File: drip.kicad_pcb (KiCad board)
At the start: 2 copper layers, 24 parts, among them Q1 2n2222, Q2 2n2222, Q3 2n2222, Q4 2n2222, Q5 2n2222, Q6 2n2222, Q7 2n2222, Q8 2n2222, U1 SA39-12YWA, U2 SA39-12YWA, U3 SA39-12YWA, U4 SA39-12YWA, U5 SA39-12YWA, U6 SA39-12YWA, U7 SA39-12YWA, U8 SA39-12YWA

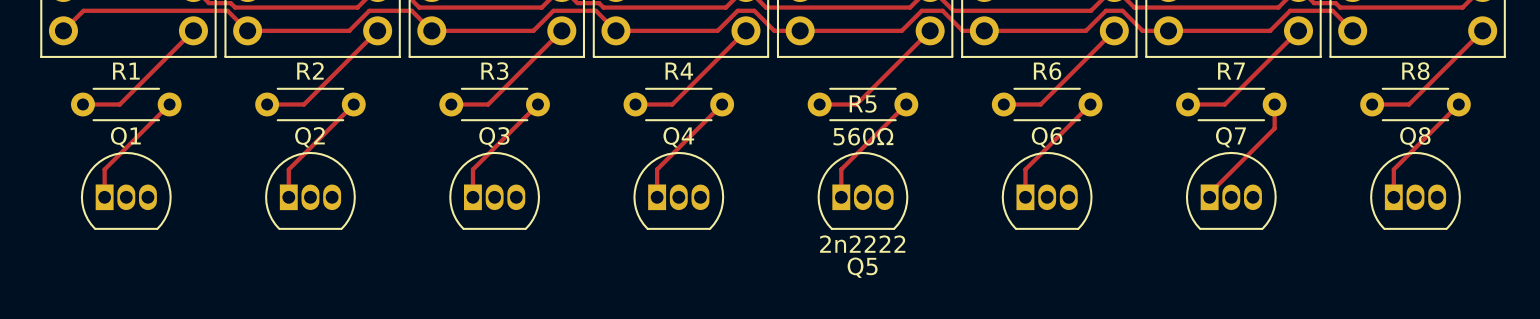
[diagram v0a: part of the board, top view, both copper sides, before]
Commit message: PNP transistors to prepare for '138 based
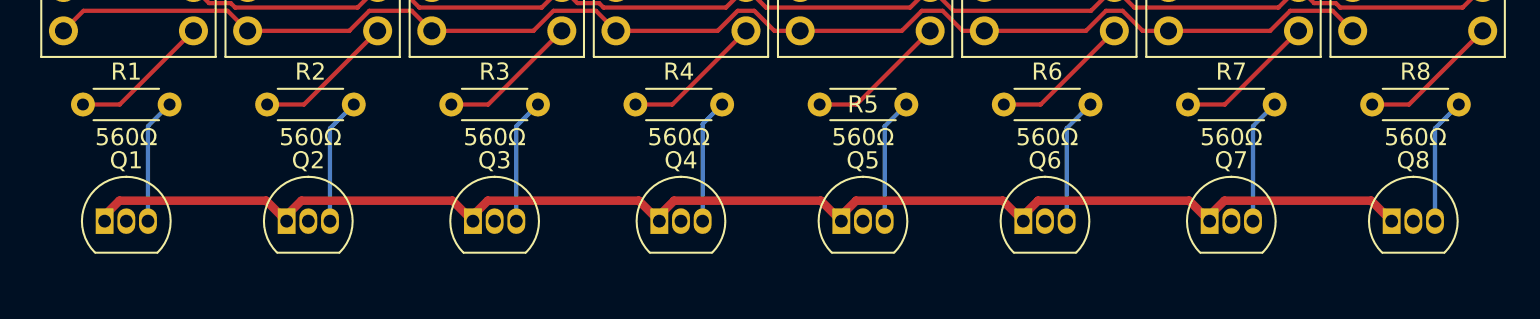
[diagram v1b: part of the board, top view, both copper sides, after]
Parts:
- Q1, Q2, Q3, Q4, Q5, Q6, Q7, Q8: value 2n2222 -> 2n2907
- moved Q2 1.40 mm to (86.9, 53.2)
- moved Q4 1.40 mm to (108.7, 53.2)
- moved Q6 1.40 mm to (130.0, 53.2)
- moved Q8 1.40 mm to (151.6, 53.2)
- moved Q1 1.40 mm to (76.2, 53.2)
- moved Q3 1.40 mm to (97.8, 53.2)
- moved Q5 1.40 mm to (119.4, 53.2)
- moved Q7 1.40 mm to (141.0, 53.2)
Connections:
- net /7SEG_A renamed Net-(R9-Pad2)
- net /7SEG_B renamed Net-(R10-Pad2)
- net /7SEG_C renamed Net-(R11-Pad2)
- net /7SEG_D renamed Net-(R12-Pad2)
- net /7SEG_E renamed Net-(R13-Pad2)
- net /7SEG_F renamed Net-(R14-Pad2)
- net /7SEG_G renamed Net-(R15-Pad2)
- Q1 pad 1: Net-(Q1-Pad1) -> +3V3
- Q1 pad 3: +3V3 -> Net-(Q1-Pad3)
- Q2 pad 1: Net-(Q2-Pad1) -> +3V3
- Q2 pad 3: +3V3 -> Net-(R2-Pad2)
- Q3 pad 1: Net-(Q3-Pad1) -> +3V3
- Q3 pad 3: +3V3 -> Net-(R3-Pad2)
- Q4 pad 1: Net-(Q4-Pad1) -> +3V3
- Q4 pad 3: +3V3 -> Net-(R4-Pad2)
- Q5 pad 1: Net-(Q5-Pad1) -> +3V3
- Q5 pad 3: +3V3 -> Net-(R5-Pad2)
- Q6 pad 1: Net-(Q6-Pad1) -> +3V3
- Q6 pad 3: +3V3 -> Net-(R6-Pad2)
- Q7 pad 1: Net-(Q7-Pad1) -> +3V3
- Q7 pad 3: +3V3 -> Net-(R7-Pad2)
- Q8 pad 1: Net-(Q8-Pad1) -> +3V3
- Q8 pad 3: +3V3 -> Net-(R8-Pad2)
- R1 pad 2: Net-(Q1-Pad1) -> Net-(Q1-Pad3)
- R2 pad 2: Net-(Q2-Pad1) -> Net-(R2-Pad2)
- R3 pad 2: Net-(Q3-Pad1) -> Net-(R3-Pad2)
- R4 pad 2: Net-(Q4-Pad1) -> Net-(R4-Pad2)
- R5 pad 2: Net-(Q5-Pad1) -> Net-(R5-Pad2)
- R6 pad 2: Net-(Q6-Pad1) -> Net-(R6-Pad2)
- R7 pad 2: Net-(Q7-Pad1) -> Net-(R7-Pad2)
- R8 pad 2: Net-(Q8-Pad1) -> Net-(R8-Pad2)
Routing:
- net +3V3: track 0.00 -> 83.8 mm
- net Net-(R6-Pad2): track 0.00 -> 7.42 mm
- net Net-(R2-Pad2): track 0.00 -> 7.42 mm
- net Net-(R8-Pad2): track 0.00 -> 7.42 mm
- net Net-(R7-Pad2): track 0.00 -> 7.36 mm
- net Net-(Q1-Pad3): track 0.00 -> 7.36 mm
- net Net-(R5-Pad2): track 0.00 -> 7.36 mm
- net Net-(R3-Pad2): track 0.00 -> 7.36 mm
- net Net-(R4-Pad2): track 0.00 -> 7.31 mm
- net Net-(Q8-Pad1): track 7.02 -> 0.00 mm
- net Net-(Q7-Pad1): track 7.02 -> 0.00 mm
- net Net-(Q6-Pad1): track 7.02 -> 0.00 mm
- net Net-(Q5-Pad1): track 7.02 -> 0.00 mm
- net Net-(Q4-Pad1): track 7.02 -> 0.00 mm
- net Net-(Q2-Pad1): track 7.02 -> 0.00 mm
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
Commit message: Add a ridiculous logo
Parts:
- added G***: LOGO, Logos:LittleDrip30mm, F.Cu at (78.5, 89.2)
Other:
- board text added: "leadedsolder.com 2023"

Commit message: LED driver done
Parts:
- removed R1, R2, R3, R4, R5, R6, R7, R8: 560Ω, Resistor_THT:R_Axial_DIN0204_L3.6mm_D1.6mm_P5.08mm_Horizontal
- removed U5, U6, U7, U8: SA39-12YWA, Display_7Segment:Sx39-1xxxxx
- added J1: ISP, Connector_PinHeader_2.54mm:PinHeader_1x04_P2.54mm_Vertical, F.Cu at (95.2, 34.9)
- added JP1: Jumper_2_Bridged, Jumper:SolderJumper-2_P1.3mm_Bridged2Bar_RoundedPad1.0x1.5mm, F.Cu at (168.4, 126.5)
- added JP2: Jumper_2_Bridged, Jumper:SolderJumper-2_P1.3mm_Bridged2Bar_RoundedPad1.0x1.5mm, F.Cu at (171.2, 126.5)
- added JP3: Jumper_2_Bridged, Jumper:SolderJumper-2_P1.3mm_Bridged2Bar_RoundedPad1.0x1.5mm, F.Cu at (174.0, 126.5)
- added JP4: Jumper_2_Bridged, Jumper:SolderJumper-2_P1.3mm_Bridged2Bar_RoundedPad1.0x1.5mm, F.Cu at (176.8, 126.5)
- added SW1: 8, Button_Switch_Keyboard:SW_Cherry_MX_1.00u_PCB, F.Cu at (172.1, 43.0)
- added SW10: Divide, Button_Switch_Keyboard:SW_Cherry_MX_1.00u_PCB, F.Cu at (132.4, 56.2)
- added SW11: Divide, Button_Switch_Keyboard:SW_Cherry_MX_1.00u_PCB, F.Cu at (152.6, 63.2)
- added SW12: Divide, Button_Switch_Keyboard:SW_Cherry_MX_1.00u_PCB, F.Cu at (213.2, 56.4)
- added SW2: 5, Button_Switch_Keyboard:SW_Cherry_MX_1.00u_PCB, F.Cu at (183.0, 16.0)
- added SW3: 2, Button_Switch_Keyboard:SW_Cherry_MX_1.00u_PCB, F.Cu at (212.5, 36.2)
- added SW4: Decimal, Button_Switch_Keyboard:SW_Cherry_MX_1.00u_PCB, F.Cu at (223.4, 16.0)
- added SW5: 9, Button_Switch_Keyboard:SW_Cherry_MX_1.00u_PCB, F.Cu at (232.7, 36.2)
- added SW6: 6, Button_Switch_Keyboard:SW_Cherry_MX_1.00u_PCB, F.Cu at (172.8, 63.2)
- added SW7: 3, Button_Switch_Keyboard:SW_Cherry_MX_1.00u_PCB, F.Cu at (193.0, 56.4)
- added SW8: CHS, Button_Switch_Keyboard:SW_Cherry_MX_1.00u_PCB, F.Cu at (192.3, 36.2)
- added SW9: Divide, Button_Switch_Keyboard:SW_Cherry_MX_1.00u_PCB, F.Cu at (203.2, 16.0)
- U1: value SA39-12YWA -> 74LS138; footprint Display_7Segment:Sx39-1xxxxx -> Package_DIP:DIP-16_W7.62mm_Socket_LongPads
- U2, U3: value SA39-12YWA -> 5641AS-4Digit-7Segment; footprint Display_7Segment:Sx39-1xxxxx -> 5641AS:5641AS_THT
- U4: value SA39-12YWA -> MSP430G2553IN20; footprint Display_7Segment:Sx39-1xxxxx -> Package_DIP:DIP-20_W7.62mm
- moved G*** 133.8 mm to (204.9, 133.2)
- moved U1 131.4 mm to (176.8, 113.5), turned to -90 degrees
- moved U3 121.1 mm to (188.6, 109.2)
- moved U4 102.9 mm to (129.5, 132.1), turned to 90 degrees
- moved U2 94.1 mm to (138.1, 109.2)
- moved Q5 88.7 mm to (182.4, 115.6)
- moved Q6 85.1 mm to (188.0, 115.6)
- moved Q1 84.2 mm to (132.7, 115.6)
- moved Q7 81.6 mm to (193.5, 115.6)
- moved Q2 80.8 mm to (138.2, 115.6)
- moved Q8 78.4 mm to (199.1, 115.6)
- moved Q3 77.5 mm to (143.8, 115.6)
- moved Q4 74.4 mm to (149.4, 115.6)
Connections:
- Q1 pad 1: +3V3 -> GND
- Q1 pad 2: unconnected-(Q1-Pad2) -> Net-(Q1-Pad2)
- Q2 pad 1: +3V3 -> GND
- Q2 pad 2: unconnected-(Q2-Pad2) -> Net-(Q2-Pad2)
- Q2 pad 3: Net-(R2-Pad2) -> Net-(Q2-Pad3)
- Q3 pad 1: +3V3 -> GND
- Q3 pad 2: unconnected-(Q3-Pad2) -> Net-(Q3-Pad2)
- Q3 pad 3: Net-(R3-Pad2) -> Net-(Q3-Pad3)
- Q4 pad 1: +3V3 -> GND
- Q4 pad 2: unconnected-(Q4-Pad2) -> Net-(Q4-Pad2)
- Q4 pad 3: Net-(R4-Pad2) -> Net-(Q4-Pad3)
- Q5 pad 1: +3V3 -> GND
- Q5 pad 2: unconnected-(Q5-Pad2) -> Net-(Q5-Pad2)
- Q5 pad 3: Net-(R5-Pad2) -> Net-(Q5-Pad3)
- Q6 pad 1: +3V3 -> GND
- Q6 pad 2: unconnected-(Q6-Pad2) -> Net-(Q6-Pad2)
- Q6 pad 3: Net-(R6-Pad2) -> Net-(Q6-Pad3)
- Q7 pad 1: +3V3 -> GND
- Q7 pad 2: unconnected-(Q7-Pad2) -> Net-(Q7-Pad2)
- Q7 pad 3: Net-(R7-Pad2) -> Net-(Q7-Pad3)
- Q8 pad 1: +3V3 -> GND
- Q8 pad 2: unconnected-(Q8-Pad2) -> Net-(Q8-Pad2)
- Q8 pad 3: Net-(R8-Pad2) -> Net-(Q8-Pad3)
- U1 pad 1: unconnected-(U1-Pad1) -> Net-(JP4-Pad2)
- U1 pad 10: Net-(R9-Pad2) -> Net-(R3-Pad1)
- U1 pad 2: Net-(R14-Pad2) -> Net-(JP3-Pad2)
- U1 pad 3: Net-(R15-Pad2) -> Net-(JP2-Pad2)
- U1 pad 4: Net-(R13-Pad2) -> GND
- U1 pad 5: Net-(R12-Pad2) -> Net-(JP1-Pad2)
- U1 pad 6: Net-(R1-Pad1) -> VCC
- U1 pad 7: GND -> Net-(R1-Pad1)
- U1 pad 8: Net-(R11-Pad2) -> GND
- U1 pad 9: Net-(R10-Pad2) -> Net-(R2-Pad1)
- U2 pad 1: unconnected-(U2-Pad1) -> /d4
- U2 pad 10: Net-(R9-Pad2) -> /d5
- U2 pad 2: Net-(R14-Pad2) -> /d3
- U2 pad 3: Net-(R15-Pad2) -> /d7
- U2 pad 4: Net-(R13-Pad2) -> /d2
- U2 pad 5: Net-(R12-Pad2) -> /d6
- U2 pad 6: Net-(R2-Pad1) -> Net-(Q4-Pad3)
- U2 pad 7: GND -> /d1
- U2 pad 8: Net-(R11-Pad2) -> Net-(Q3-Pad3)
- U2 pad 9: Net-(R10-Pad2) -> Net-(Q2-Pad3)
- U3 pad 1: unconnected-(U3-Pad1) -> /d4
- U3 pad 10: Net-(R9-Pad2) -> /d5
- U3 pad 2: Net-(R14-Pad2) -> /d3
- U3 pad 3: Net-(R15-Pad2) -> /d7
- U3 pad 4: Net-(R13-Pad2) -> /d2
- U3 pad 5: Net-(R12-Pad2) -> /d6
- U3 pad 6: Net-(R3-Pad1) -> Net-(Q8-Pad3)
- U3 pad 7: GND -> /d1
- U3 pad 8: Net-(R11-Pad2) -> Net-(Q7-Pad3)
- U3 pad 9: Net-(R10-Pad2) -> Net-(Q6-Pad3)
- U4 pad 1: unconnected-(U4-Pad1) -> VCC
- U4 pad 10: Net-(R9-Pad2) -> unconnected-(U4-Pad10)
- U4 pad 2: Net-(R14-Pad2) -> /d0
- U4 pad 3: Net-(R15-Pad2) -> /d1
- U4 pad 4: Net-(R13-Pad2) -> /d2
- U4 pad 5: Net-(R12-Pad2) -> /d3
- U4 pad 6: Net-(R4-Pad1) -> /d4
- U4 pad 7: GND -> /d5
- U4 pad 8: Net-(R11-Pad2) -> unconnected-(U4-Pad8)
- U4 pad 9: Net-(R10-Pad2) -> unconnected-(U4-Pad9)
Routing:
- net +3V3: track 83.8 -> 0.00 mm
- net Net-(R10-Pad2): track 82.7 -> 0.00 mm
- net Net-(R15-Pad2): track 82.5 -> 0.00 mm
- net GND: track 82.5 -> 0.00 mm
- net Net-(R9-Pad2): track 82.4 -> 0.00 mm
- net Net-(R12-Pad2): track 82.4 -> 0.00 mm
- net Net-(R13-Pad2): track 82.4 -> 0.00 mm
- net Net-(R11-Pad2): track 82.4 -> 0.00 mm
- net Net-(R14-Pad2): track 82.4 -> 0.00 mm
- net Net-(JP4-Pad2): track 0.00 -> 13.2 mm, vias 0 -> 1
- net Net-(JP3-Pad2): track 0.00 -> 13.1 mm, vias 0 -> 1
- net Net-(JP1-Pad2): track 0.00 -> 13.0 mm, vias 0 -> 1
- net Net-(JP2-Pad2): track 0.00 -> 13.0 mm, vias 0 -> 1
- net Net-(R7-Pad1): track 8.27 -> 0.00 mm
- net Net-(R3-Pad1): track 8.27 -> 0.00 mm
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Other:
- board text added: "5641AS"

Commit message: Button footprint, maybe
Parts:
- added R1: 10kΩ, Resistor_THT:R_Axial_DIN0207_L6.3mm_D2.5mm_P10.16mm_Horizontal, F.Cu at (266.2, 154.0)
- added R10: 10kΩ, Resistor_THT:R_Axial_DIN0207_L6.3mm_D2.5mm_P10.16mm_Horizontal, F.Cu at (292.8, 141.9)
- added R11: 47kΩ, Resistor_THT:R_Axial_DIN0207_L6.3mm_D2.5mm_P10.16mm_Horizontal, F.Cu at (266.2, 145.9)
- added R12: 10kΩ, Resistor_THT:R_Axial_DIN0207_L6.3mm_D2.5mm_P10.16mm_Horizontal, F.Cu at (254.4, 176.1)
- added R13: 10kΩ, Resistor_THT:R_Axial_DIN0207_L6.3mm_D2.5mm_P10.16mm_Horizontal, F.Cu at (266.2, 158.1)
- added R14: 10kΩ, Resistor_THT:R_Axial_DIN0207_L6.3mm_D2.5mm_P10.16mm_Horizontal, F.Cu at (267.8, 150.0)
- added R15: 10kΩ, Resistor_THT:R_Axial_DIN0207_L6.3mm_D2.5mm_P10.16mm_Horizontal, F.Cu at (267.8, 162.1)
- added R16: 10kΩ, Resistor_THT:R_Axial_DIN0207_L6.3mm_D2.5mm_P10.16mm_Horizontal, F.Cu at (254.4, 163.9)
- added R17: 10kΩ, Resistor_THT:R_Axial_DIN0207_L6.3mm_D2.5mm_P10.16mm_Horizontal, F.Cu at (279.5, 141.9)
- added R18: 10kΩ, Resistor_THT:R_Axial_DIN0207_L6.3mm_D2.5mm_P10.16mm_Horizontal, F.Cu at (281.1, 150.0)
- added R19: 10kΩ, Resistor_THT:R_Axial_DIN0207_L6.3mm_D2.5mm_P10.16mm_Horizontal, F.Cu at (254.4, 168.0)
- added R2: 10kΩ, Resistor_THT:R_Axial_DIN0207_L6.3mm_D2.5mm_P10.16mm_Horizontal, F.Cu at (254.4, 180.1)
- added R3: 10kΩ, Resistor_THT:R_Axial_DIN0207_L6.3mm_D2.5mm_P10.16mm_Horizontal, F.Cu at (292.8, 145.9)
- added R4: 10kΩ, Resistor_THT:R_Axial_DIN0207_L6.3mm_D2.5mm_P10.16mm_Horizontal, F.Cu at (254.4, 172.0)
- added R5: 10kΩ, Resistor_THT:R_Axial_DIN0207_L6.3mm_D2.5mm_P10.16mm_Horizontal, F.Cu at (266.2, 141.9)
- added R6: 10kΩ, Resistor_THT:R_Axial_DIN0207_L6.3mm_D2.5mm_P10.16mm_Horizontal, F.Cu at (279.5, 145.9)
- added R7: 10kΩ, Resistor_THT:R_Axial_DIN0207_L6.3mm_D2.5mm_P10.16mm_Horizontal, F.Cu at (279.5, 154.0)
- added R8: 10kΩ, Resistor_THT:R_Axial_DIN0207_L6.3mm_D2.5mm_P10.16mm_Horizontal, F.Cu at (267.8, 170.2)
- added R9: 1kΩ, Resistor_THT:R_Axial_DIN0207_L6.3mm_D2.5mm_P10.16mm_Horizontal, F.Cu at (267.8, 166.2)
- added SW13: 7, DripButtons:8mm_G77_Push, F.Cu at (267.4, 183.4)
- added SW14: 4, DripButtons:8mm_G77_Push, F.Cu at (322.8, 168.8)
- added SW15: 1, DripButtons:8mm_G77_Push, F.Cu at (280.7, 167.2)
- added SW16: 0, DripButtons:8mm_G77_Push, F.Cu at (254.1, 184.3)
- added SW17: Hex, DripButtons:8mm_G77_Push, F.Cu at (337.4, 142.0)
- added SW18: E, DripButtons:8mm_G77_Push, F.Cu at (275.2, 193.9)
- added SW19: B, DripButtons:8mm_G77_Push, F.Cu at (313.5, 159.9)
- added SW20: 8, DripButtons:8mm_G77_Push, F.Cu at (299.0, 189.9)
- added SW21: 5, DripButtons:8mm_G77_Push, F.Cu at (316.3, 142.0)
- added SW22: 2, DripButtons:8mm_G77_Push, F.Cu at (324.1, 151.0)
- added SW23: Decimal, DripButtons:8mm_G77_Push, F.Cu at (278.0, 185.0)
- added SW24: Oct, DripButtons:8mm_G77_Push, F.Cu at (291.3, 163.1)
- added SW25: F, DripButtons:8mm_G77_Push, F.Cu at (264.6, 192.3)
- added SW26: C, DripButtons:8mm_G77_Push, F.Cu at (345.1, 151.0)
- added SW27: 9, DripButtons:8mm_G77_Push, F.Cu at (347.9, 142.0)
- added SW28: 6, DripButtons:8mm_G77_Push, F.Cu at (312.3, 168.8)
- added SW29: 3, DripButtons:8mm_G77_Push, F.Cu at (301.8, 168.8)
- added SW30: +/-, DripButtons:8mm_G77_Push, F.Cu at (313.5, 151.0)
- added SW31: Clear, DripButtons:8mm_G77_Push, F.Cu at (291.3, 172.0)
- added SW32: K, DripButtons:8mm_G77_Push, F.Cu at (280.7, 158.2)
- added SW33: Div, DripButtons:8mm_G77_Push, F.Cu at (334.6, 151.0)
- added SW34: Mul, DripButtons:8mm_G77_Push, F.Cu at (278.0, 176.1)
- added SW35: Minus, DripButtons:8mm_G77_Push, F.Cu at (326.8, 142.0)
- added SW36: Plus, DripButtons:8mm_G77_Push, F.Cu at (303.0, 159.9)
- added SW37: Enter, DripButtons:8mm_G77_Push, F.Cu at (305.8, 142.0)
- added U7: 74HC595, Package_DIP:DIP-16_W7.62mm_Socket_LongPads, F.Cu at (254.9, 142.0)
- SW1: value 8 -> Bin; footprint Button_Switch_Keyboard:SW_Cherry_MX_1.00u_PCB -> DripButtons:8mm_G77_Push
- SW10: value Divide -> Recall; footprint Button_Switch_Keyboard:SW_Cherry_MX_1.00u_PCB -> DripButtons:8mm_G77_Push
- SW11: value Divide -> D; footprint Button_Switch_Keyboard:SW_Cherry_MX_1.00u_PCB -> DripButtons:8mm_G77_Push
- SW12: value Divide -> A; footprint Button_Switch_Keyboard:SW_Cherry_MX_1.00u_PCB -> DripButtons:8mm_G77_Push
- SW2: value 5 -> Store; footprint Button_Switch_Keyboard:SW_Cherry_MX_1.00u_PCB -> DripButtons:8mm_G77_Push
- SW3: value 2 -> Shift; footprint Button_Switch_Keyboard:SW_Cherry_MX_1.00u_PCB -> DripButtons:8mm_G77_Push
- SW4: value Decimal -> 1'sCompl; footprint Button_Switch_Keyboard:SW_Cherry_MX_1.00u_PCB -> DripButtons:8mm_G77_Push
- SW5: value 9 -> Or; footprint Button_Switch_Keyboard:SW_Cherry_MX_1.00u_PCB -> DripButtons:8mm_G77_Push
- SW6: value 6 -> And; footprint Button_Switch_Keyboard:SW_Cherry_MX_1.00u_PCB -> DripButtons:8mm_G77_Push
- SW7: value 3 -> Xor; footprint Button_Switch_Keyboard:SW_Cherry_MX_1.00u_PCB -> DripButtons:8mm_G77_Push
- SW8: value CHS -> Clear Entry; footprint Button_Switch_Keyboard:SW_Cherry_MX_1.00u_PCB -> DripButtons:8mm_G77_Push
- SW9: value Divide -> Dec; footprint Button_Switch_Keyboard:SW_Cherry_MX_1.00u_PCB -> DripButtons:8mm_G77_Push
- U1: value 74LS138 -> 74HC138
- moved SW10 219.9 mm to (309.5, 186.6)
- moved SW2 209.0 mm to (334.6, 159.9)
- moved SW1 192.4 mm to (309.5, 177.7)
- moved SW6 186.5 mm to (320.0, 177.7)
- moved SW4 185.7 mm to (288.5, 189.9)
- moved SW8 180.7 mm to (324.1, 159.9)
- moved SW9 171.0 mm to (267.4, 174.4)
- moved SW11 165.0 mm to (254.1, 193.3)
- moved SW7 163.5 mm to (299.0, 181.0)
- moved SW5 155.1 mm to (288.5, 181.0)
- moved SW3 142.5 mm to (292.5, 154.2)
- moved SW12 130.4 mm to (303.0, 151.0)
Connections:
- JP2 pad 1: /~{LED_SEL_2} -> /SEL_2
- JP3 pad 1: /~{LED_SEL_1} -> /SEL_1
- JP4 pad 1: /~{LED_SEL_0} -> /SEL_0
- SW1 pad 1: unconnected-(SW1-Pad1) -> /KBD_ROW_0
- SW1 pad 2: unconnected-(SW1-Pad2) -> /~{KBD_COL_0}
- SW10 pad 1: unconnected-(SW10-Pad1) -> /KBD_ROW_1
- SW10 pad 2: unconnected-(SW10-Pad2) -> /~{KBD_COL_1}
- SW11 pad 1: unconnected-(SW11-Pad1) -> /KBD_ROW_2
- SW11 pad 2: unconnected-(SW11-Pad2) -> /~{KBD_COL_1}
- SW12 pad 1: unconnected-(SW12-Pad1) -> /KBD_ROW_3
- SW12 pad 2: unconnected-(SW12-Pad2) -> /~{KBD_COL_1}
- SW2 pad 1: unconnected-(SW2-Pad1) -> /KBD_ROW_1
- SW2 pad 2: unconnected-(SW2-Pad2) -> /~{KBD_COL_0}
- SW3 pad 1: unconnected-(SW3-Pad1) -> /KBD_ROW_2
- SW3 pad 2: unconnected-(SW3-Pad2) -> /~{KBD_COL_0}
- SW4 pad 1: unconnected-(SW4-Pad1) -> /KBD_ROW_3
- SW4 pad 2: unconnected-(SW4-Pad2) -> /~{KBD_COL_0}
- SW5 pad 1: unconnected-(SW5-Pad1) -> /KBD_ROW_4
- SW5 pad 2: unconnected-(SW5-Pad2) -> /~{KBD_COL_0}
- SW6 pad 1: unconnected-(SW6-Pad1) -> /KBD_ROW_5
- SW6 pad 2: unconnected-(SW6-Pad2) -> /~{KBD_COL_0}
- SW7 pad 1: unconnected-(SW7-Pad1) -> /KBD_ROW_6
- SW7 pad 2: unconnected-(SW7-Pad2) -> /~{KBD_COL_0}
- SW8 pad 1: unconnected-(SW8-Pad1) -> /KBD_ROW_7
- SW8 pad 2: unconnected-(SW8-Pad2) -> /~{KBD_COL_0}
- SW9 pad 1: unconnected-(SW9-Pad1) -> /KBD_ROW_0
- SW9 pad 2: unconnected-(SW9-Pad2) -> /~{KBD_COL_1}
- U1 pad 4: GND -> /~{LED}/KBD
- U2 pad 1: /d4 -> Net-(U2-Pad1)
- U2 pad 10: /d5 -> Net-(U2-Pad10)
- U2 pad 11: /d0 -> Net-(U2-Pad11)
- U2 pad 2: /d3 -> Net-(U2-Pad2)
- U2 pad 3: /d7 -> Net-(U2-Pad3)
- U2 pad 4: /d2 -> Net-(U2-Pad4)
- U2 pad 5: /d6 -> Net-(U2-Pad5)
- U2 pad 7: /d1 -> Net-(U2-Pad7)
- U3 pad 1: /d4 -> Net-(U2-Pad1)
- U3 pad 10: /d5 -> Net-(U2-Pad10)
- U3 pad 11: /d0 -> Net-(U2-Pad11)
- U3 pad 2: /d3 -> Net-(U2-Pad2)
- U3 pad 3: /d7 -> Net-(U2-Pad3)
- U3 pad 4: /d2 -> Net-(U2-Pad4)
- U3 pad 5: /d6 -> Net-(U2-Pad5)
- U3 pad 7: /d1 -> Net-(U2-Pad7)
- U4 pad 10: unconnected-(U4-Pad10) -> /~{KBD_ROW_SEL_B}
- U4 pad 11: unconnected-(U4-Pad11) -> /~{KBD_ROW_SEL_C}
- U4 pad 14: /d6 -> unconnected-(U4-Pad14)
- U4 pad 15: /d7 -> unconnected-(U4-Pad15)
- U4 pad 2: /d0 -> /SEL_0
- U4 pad 3: /d1 -> /SEL_1
- U4 pad 4: /d2 -> /SEL_2
- U4 pad 5: /d3 -> /LED_DATA
- U4 pad 6: /d4 -> /LED_CLOCK
- U4 pad 7: /d5 -> /~{LED}/KBD
- U4 pad 8: unconnected-(U4-Pad8) -> /KBD_DATA
- U4 pad 9: unconnected-(U4-Pad9) -> /~{KBD_ROW_SEL_A}

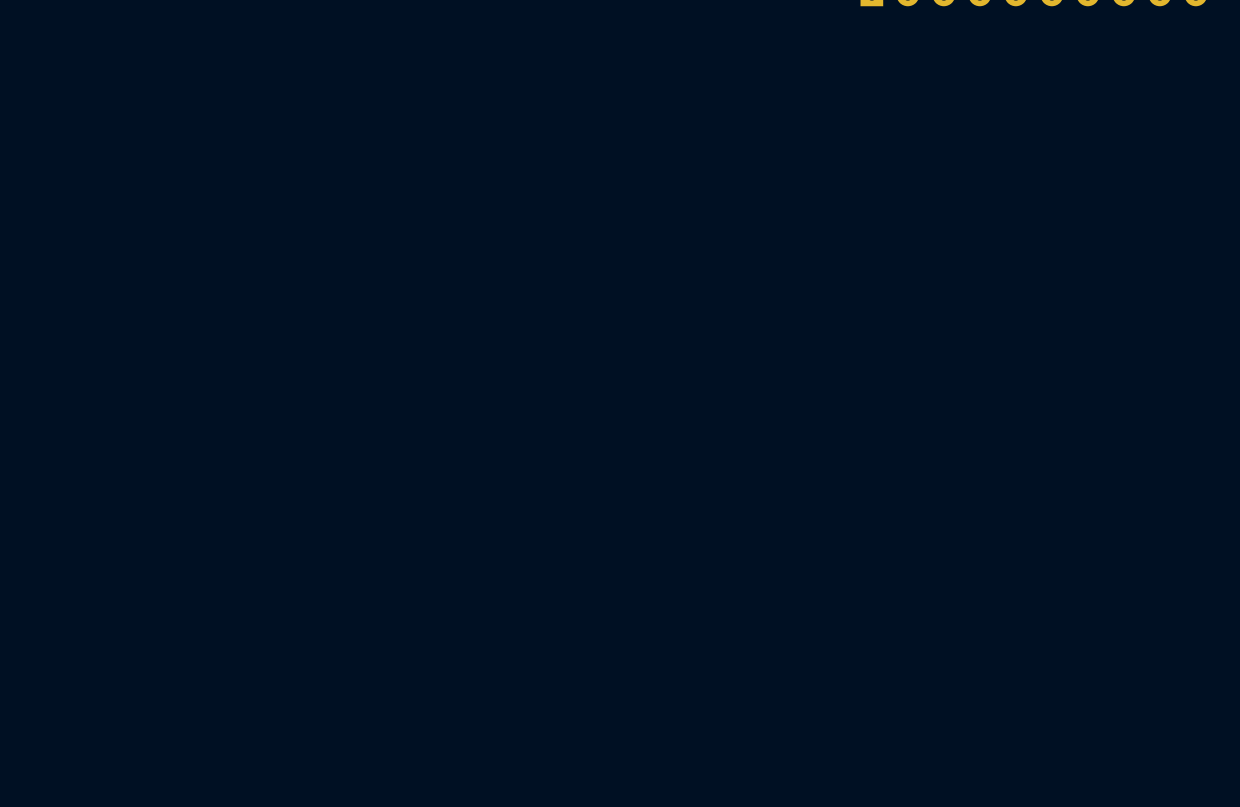
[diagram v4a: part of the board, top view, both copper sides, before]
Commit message: 2xAA holder
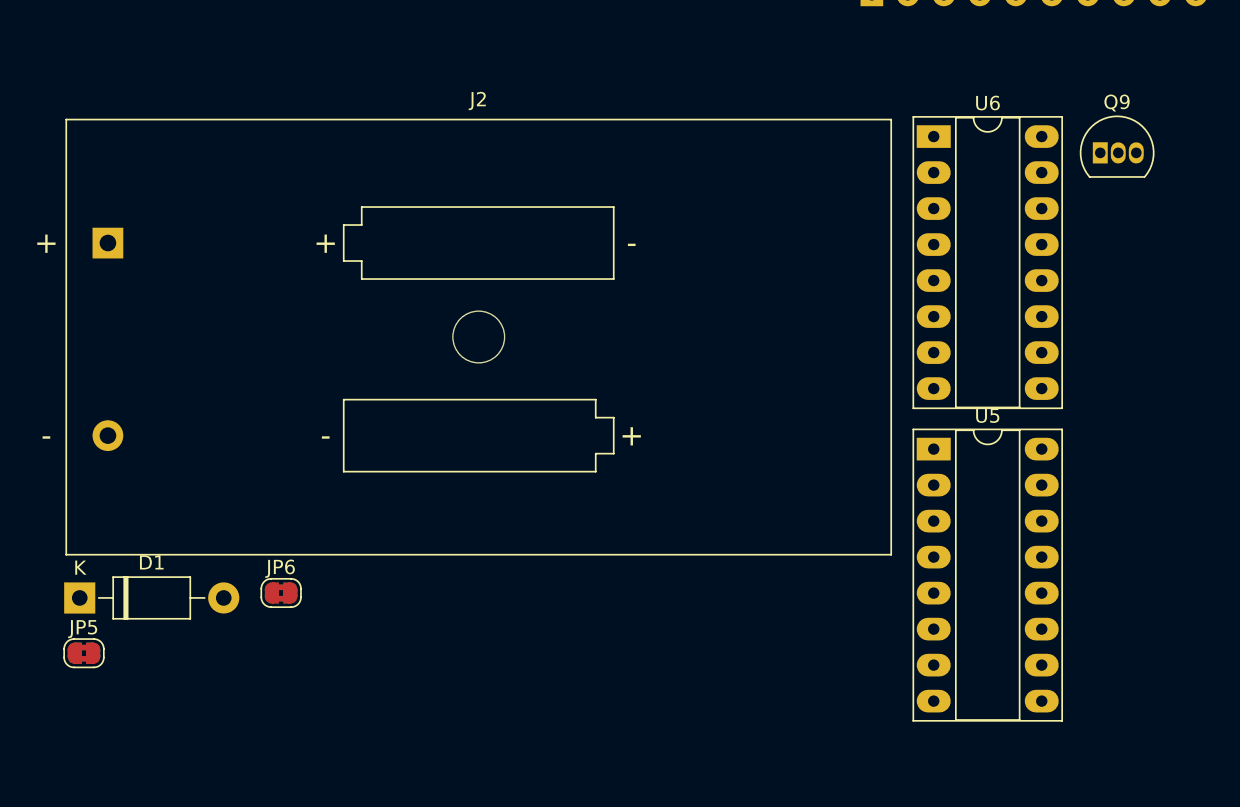
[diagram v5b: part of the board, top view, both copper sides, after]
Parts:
- added D1: 1n5817, Diode_THT:D_DO-41_SOD81_P10.16mm_Horizontal, F.Cu at (73.7, 174.6)
- added J2: 2xAA Battery Holder, Battery:BatteryHolder_MPD_BC2AAPC_2xAA, F.Cu at (75.7, 149.6)
- added JP5: Jumper_2_Bridged, Jumper:SolderJumper-2_P1.3mm_Bridged2Bar_RoundedPad1.0x1.5mm, F.Cu at (74.0, 178.5)
- added JP6: Jumper_2_Bridged, Jumper:SolderJumper-2_P1.3mm_Bridged2Bar_RoundedPad1.0x1.5mm, F.Cu at (87.9, 174.3)
- added Q9: 2n2222, Package_TO_SOT_THT:TO-92L_Inline, F.Cu at (145.7, 143.2)
- added U5: 74HC251, Package_DIP:DIP-16_W7.62mm_Socket_LongPads, F.Cu at (133.9, 164.1)
- added U6: 74HC138, Package_DIP:DIP-16_W7.62mm_Socket_LongPads, F.Cu at (133.9, 142.1)
